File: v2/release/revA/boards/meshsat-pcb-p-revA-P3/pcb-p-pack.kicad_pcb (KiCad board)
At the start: 2 copper layers, 70 x 44 mm, 60 parts, among them Q1 CSD17570Q5B 30 V N-FET, charg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, Q2 CSD17570Q5B 30 V N-FET, disch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, U1 BQ4050RSMR: SMBus 1.1 gas gau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

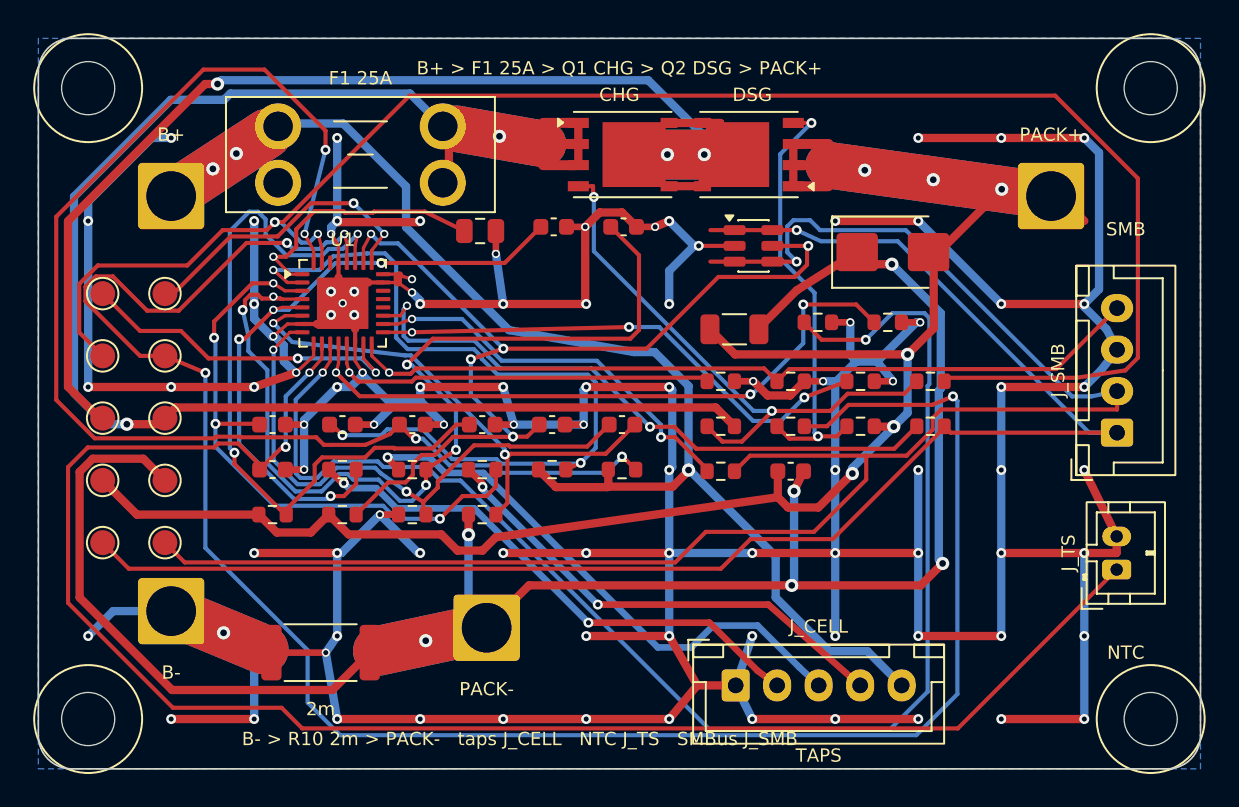
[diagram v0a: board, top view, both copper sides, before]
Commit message: feat(p): P3 re-cut and verified, the first deliverable through the collapsed finish [MESHSAT-862]
Routed on the rented box with the patched per-pass jar: 0 hard, 0 unrouted of 35 nets, 63 vias, and routeflow
ended CLEAN. The finish ran every stage in the documented order and every gate passed on the way out:
dc_drop 3 of 3 rails MET, impedance_check PASS (the board declares its pair classes and gives none a target),
netlist_board 241 of 241, check_contracts ALL PASS 40 of 40 with A present in the tree, and
verify_deliverable ALL PASS on 35 of 35 properties.

It replaces the folder cut on 9 September, which predates most of the gates that just judged this one. The
three pack connectors that refused the first attempt now carry their JST codes, and the BOM status reads OK.

The board sha256 beside the folder matches the board file in it, checked here.
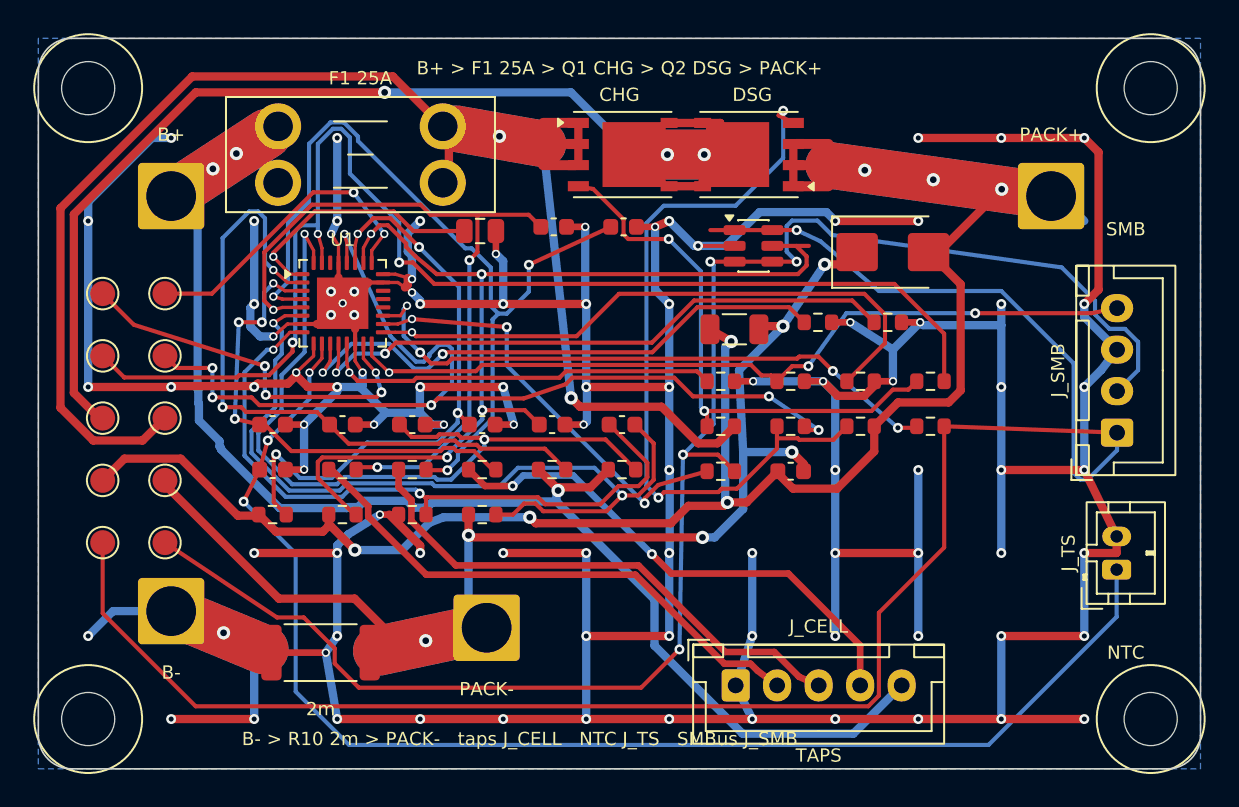
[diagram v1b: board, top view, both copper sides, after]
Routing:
- net /DSG_R: track 121.4 -> 61.5 mm, vias 4 -> 6
- net /TS2: track 86.1 -> 34.1 mm
- net /PACK_N: track 120.1 -> 80.9 mm
- net /BAT_F: track 79.1 -> 47.5 mm, vias 4 -> 2
- net /CHG_R: track 103.5 -> 77.4 mm, vias 2 -> 3
- net /SMBC: track 94.9 -> 118.0 mm
- net /TS1: track 100.6 -> 80.7 mm, vias 2 -> 3
- net /DSG_G: track 26.5 -> 45.2 mm
- net /SRN_F: track 31.4 -> 49.9 mm
- net /VC4_F: track 50.3 -> 41.3 mm, vias 3 -> 2
- net /PACK_F: track 44.5 -> 36.1 mm, vias 2 -> 4
- net /VC3_F: track 37.2 -> 28.8 mm
- net /SRP_F: track 33.8 -> 41.2 mm
- net GND: track 439.0 -> 446.4 mm
- net /SW: track 87.6 -> 81.4 mm
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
